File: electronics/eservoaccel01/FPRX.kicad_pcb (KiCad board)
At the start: 2 copper layers, 25 x 30 mm, 65 parts, among them IC3 ATMEGA328P-M, K1 CONN_3, K2 CONN_3, K3 CONN_3, K4 CONN_3, P2 CONN_1, X1 RESONATOR_16MHz

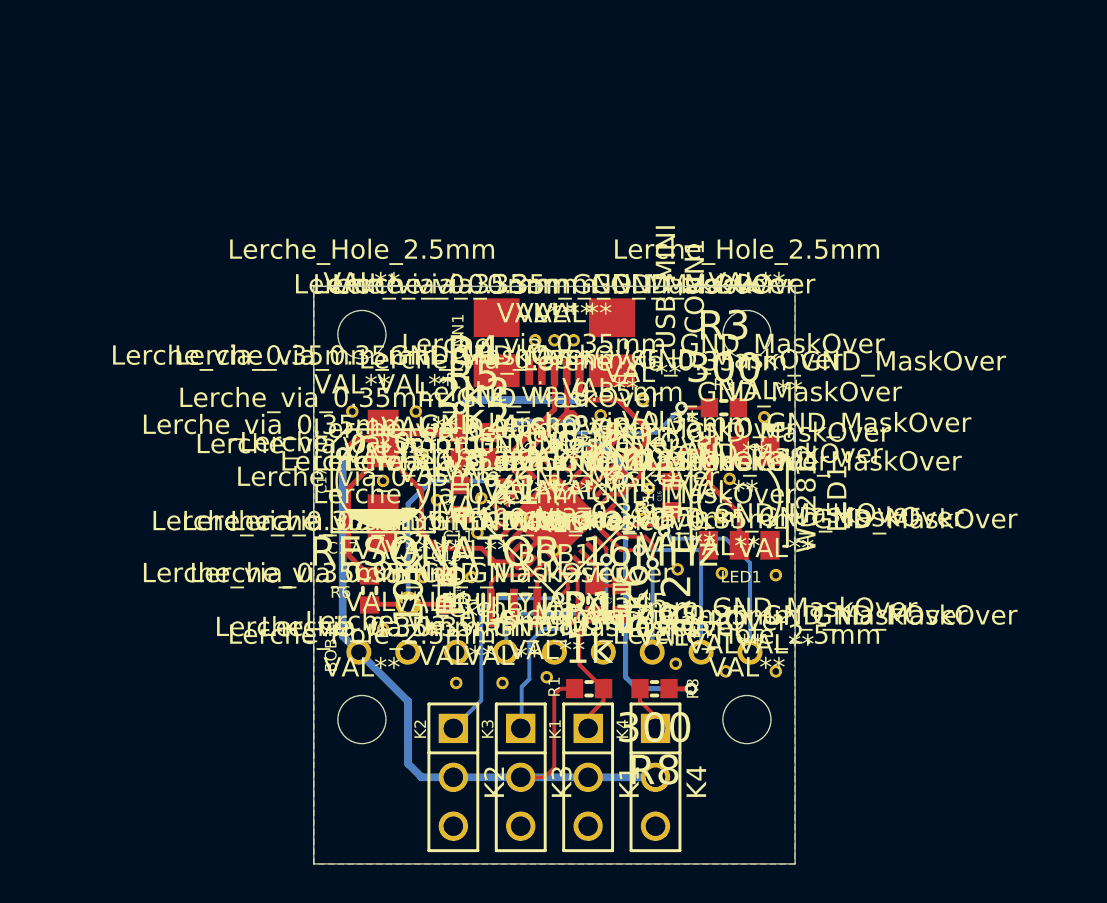
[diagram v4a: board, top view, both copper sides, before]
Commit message: Changed to Sparkfun Micro USB connector
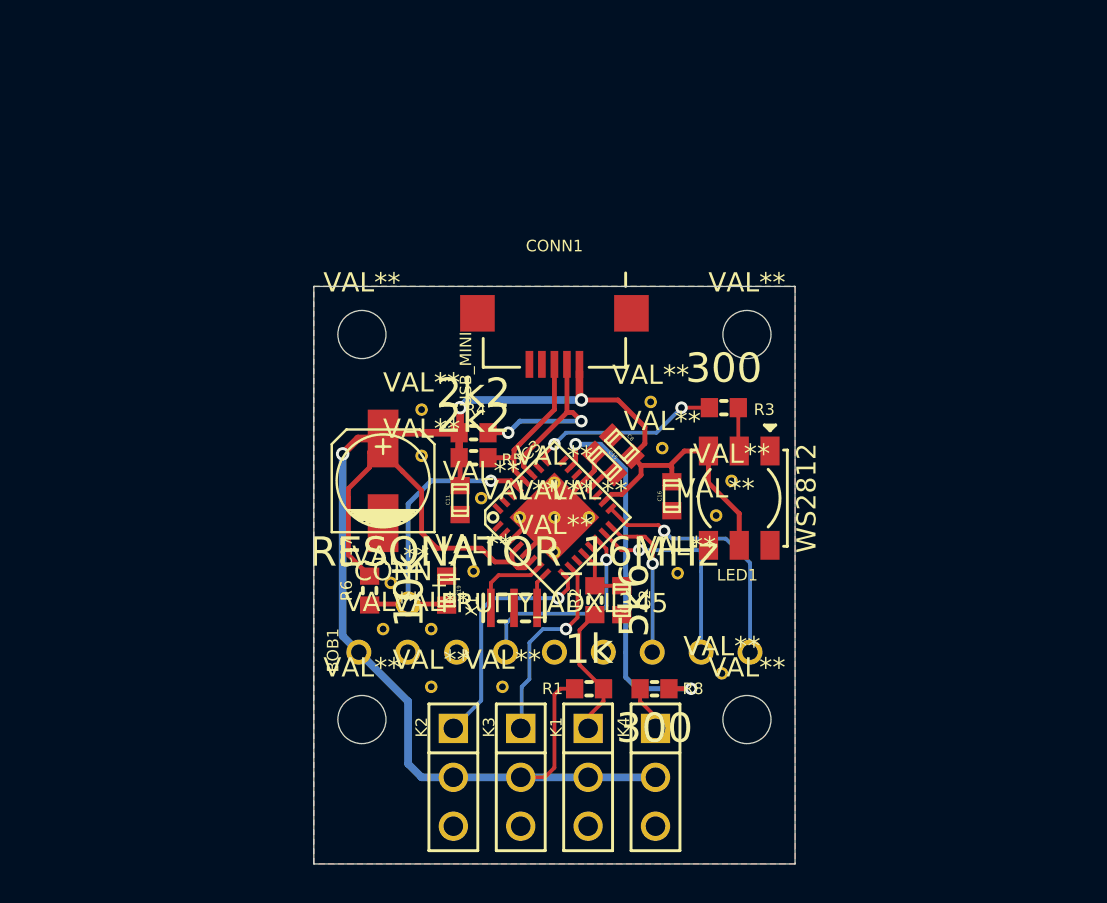
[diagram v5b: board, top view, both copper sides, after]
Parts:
- removed Lerche_Hole_2.5mm (x4): VAL**, Lerche_Hole_2.5mm
- removed Lerche_via_0.35mm_GND_MaskOver (x37): VAL**, Lerche_via_0.35mm_GND_MaskOver
- added ?: VAL**, Lerche_via_0.35mm_GND_MaskOver, F.Cu at (245.3, 144.0)
- added ?: VAL**, Lerche_via_0.35mm_GND_MaskOver, F.Cu at (243.5, 145.8)
- added ?: VAL**, Lerche_via_0.35mm_GND_MaskOver, F.Cu at (236.6, 140.8)
- added ?: VAL**, Lerche_via_0.35mm_GND_MaskOver, F.Cu at (239.7, 143.0)
- added ?: VAL**, Lerche_via_0.35mm_GND_MaskOver, F.Cu at (239.3, 146.8)
- added ?: VAL**, Lerche_via_0.35mm_GND_MaskOver, F.Cu at (235.0, 147.4)
- added ?: VAL**, Lerche_via_0.35mm_GND_MaskOver, F.Cu at (234.6, 149.8)
- added ?: VAL**, Lerche_via_0.35mm_GND_MaskOver, F.Cu at (249.9, 146.9)
- added ?: VAL**, Lerche_via_0.35mm_GND_MaskOver, F.Cu at (252.7, 142.1)
- added ?: VAL**, Lerche_via_0.35mm_GND_MaskOver, F.Cu at (251.9, 143.9)
- added ?: VAL**, Lerche_Hole_2.5mm, F.Cu at (233.5, 154.5)
- added ?: VAL**, Lerche_via_0.35mm_GND_MaskOver, F.Cu at (249.1, 140.4)
- added ?: VAL**, Lerche_via_0.35mm_GND_MaskOver, F.Cu at (248.5, 138.0)
- added ?: VAL**, Lerche_via_0.35mm_GND_MaskOver, F.Cu at (236.6, 138.4)
- added ?: VAL**, Lerche_via_0.35mm_GND_MaskOver, F.Cu at (237.1, 152.8)
- added ?: VAL**, Lerche_via_0.35mm_GND_MaskOver, F.Cu at (240.8, 152.8)
- added ?: VAL**, Lerche_via_0.35mm_GND_MaskOver, F.Cu at (252.2, 152.1)
- added ?: VAL**, Lerche_Hole_2.5mm, F.Cu at (253.5, 134.5)
- added ?: VAL**, Lerche_Hole_2.5mm, F.Cu at (233.5, 134.5)
- added ?: VAL**, Lerche_Hole_2.5mm, F.Cu at (253.5, 154.5)
- added ?: VAL**, Lerche_via_0.35mm_GND_MaskOver, F.Cu at (237.1, 149.8)
- added ?: VAL**, Lerche_via_0.35mm_GND_MaskOver, F.Cu at (243.5, 144.0)
- added ?: VAL**, Lerche_via_0.35mm_GND_MaskOver, F.Cu at (241.7, 144.0)
- added ?: VAL**, Lerche_via_0.35mm_GND_MaskOver, F.Cu at (243.5, 142.2)
- CONN1: footprint Lerche_Molex_47610-0001_Micro-USB -> Lerche_Sparkfun_MicroUSB
- moved CONN1 1.40 mm to (243.5, 133.4), turned to 180 degrees
- renumbered P2 to ?
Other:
- board text removed: "BOB1"
- board text removed: "C11"
- board text removed: "C15"
- board text removed: "C16"
- board text removed: "C17"
- board text removed: "C19"
- board text removed: "C2"
- board text removed: "C8"
- board text removed: "CONN1"
- board text removed: "IC3"
- board text removed: "K1"
- board text removed: "K2"
- board text removed: "K3"
- board text removed: "K4"
- board text removed: "LED1"
- board text removed: "R1"
- board text removed: "R2"
- board text removed: "R3"
- board text removed: "R6"
- board text removed: "R8"
- board text removed: "X1"
